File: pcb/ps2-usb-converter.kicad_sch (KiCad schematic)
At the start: 14 parts, among them J1 Mini-DIN-6

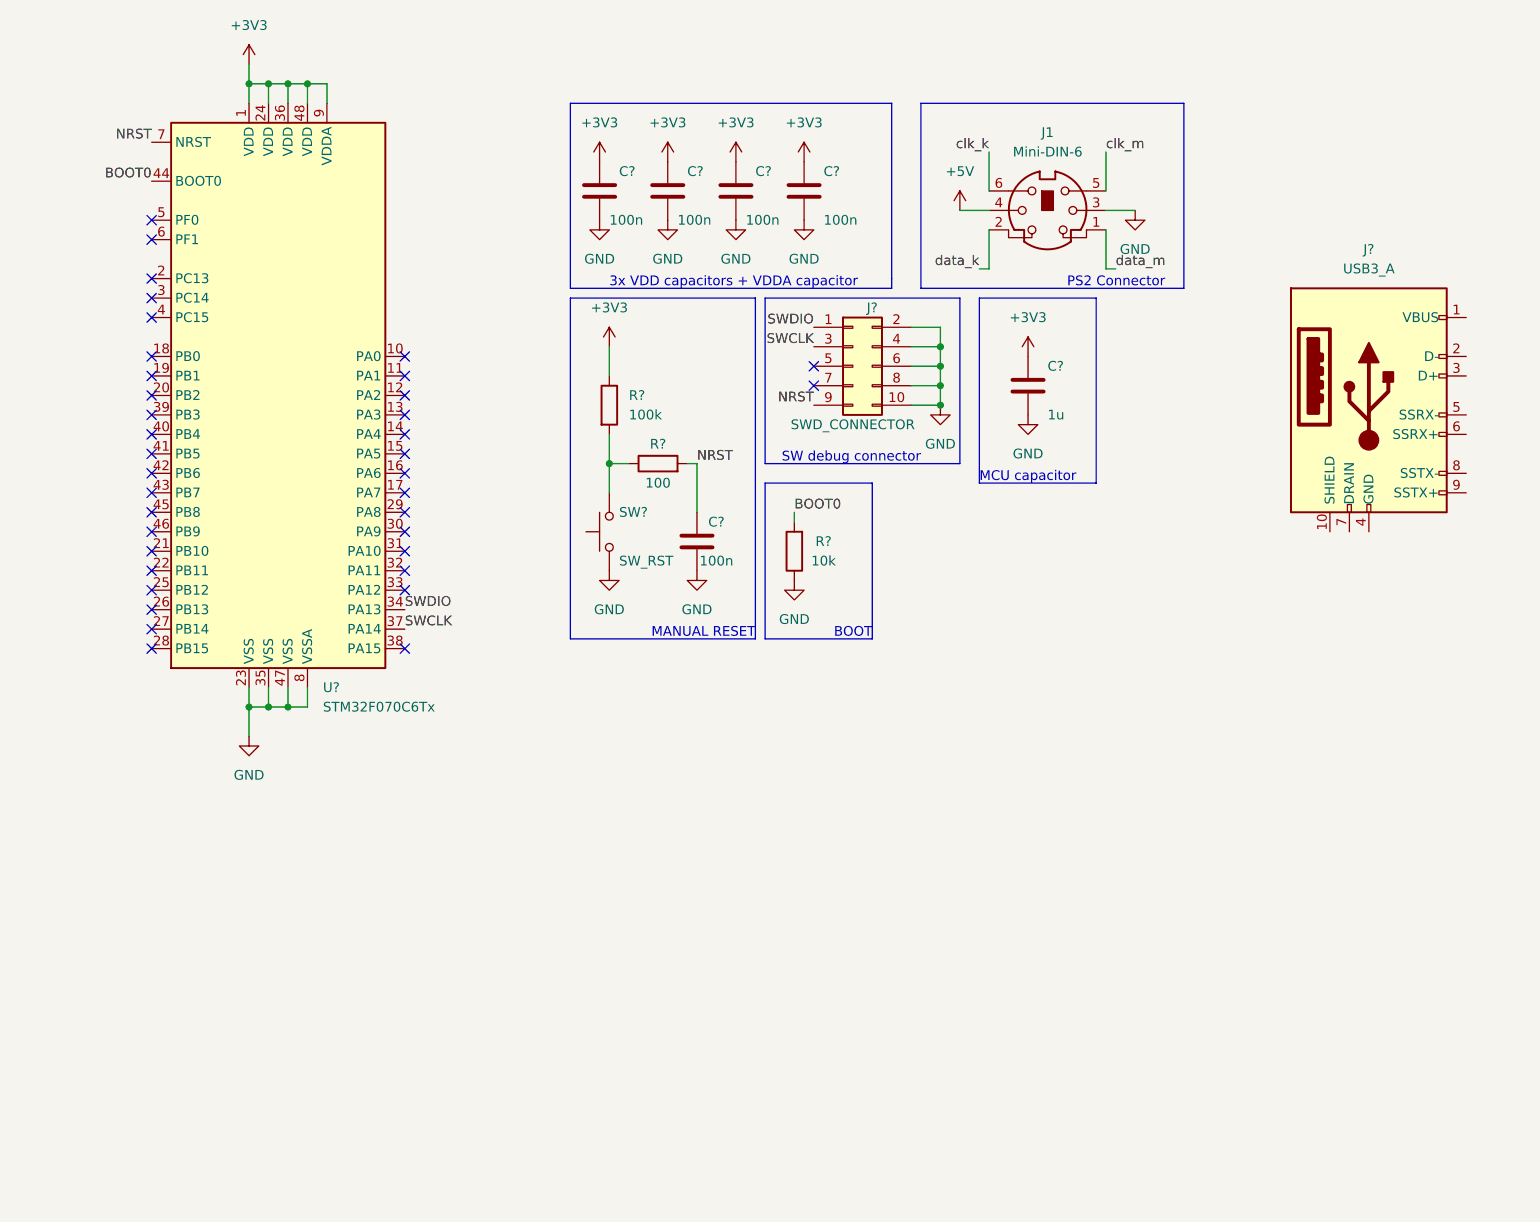
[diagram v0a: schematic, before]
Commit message: Add oscillator, power supply and usb connector to board
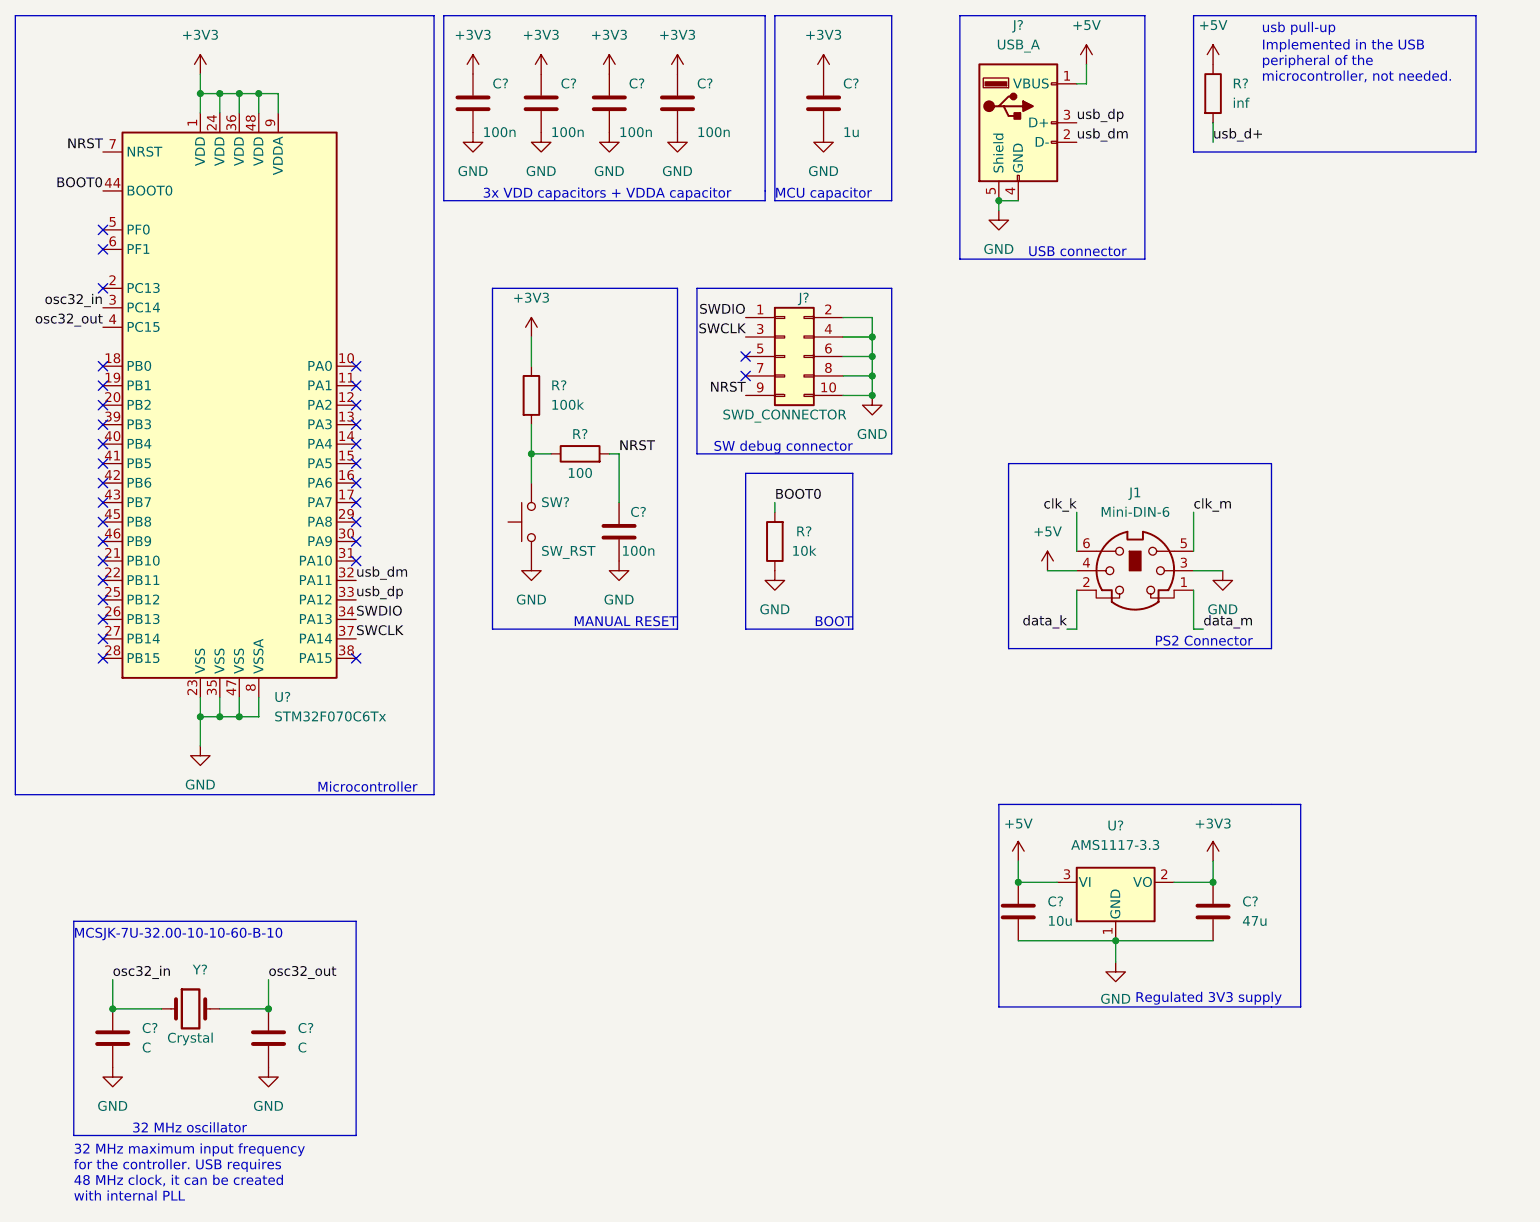
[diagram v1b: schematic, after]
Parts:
- removed J?: USB3_A, symbol Connector:USB3_A
- added C? (x2): C, symbol Device:C
- added C?: 10u, Capacitor_SMD:C_0805_2012Metric_Pad1.18x1.45mm_HandSolder, symbol Device:C
- added C?: 47u, Capacitor_SMD:C_0805_2012Metric_Pad1.18x1.45mm_HandSolder, symbol Device:C
- added J?: USB_A, symbol Connector:USB_A
- added R?: inf, symbol Device:R
- added U?: AMS1117-3.3, Package_TO_SOT_SMD:SOT-223-3_TabPin2, symbol Regulator_Linear:AMS1117-3.3
- added Y?: Crystal, symbol Device:Crystal
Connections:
- net +3V3: now also C?.1, U?.2 (VO)
- net +5V: now also C?.1, J?.1 (VBUS), R?.1, U?.3 (VI)
- net GND: now also C?.2, C?.2, C?.2, C?.2, J?.4 (GND), J?.5 (Shield), U?.1 (GND)
- net osc32_in: now reaches U?.3 (PC14)
- net osc32_in: now also C?.1, Y?.1
- net usb_dm: now reaches U?.32 (PA11)
- net usb_dm: now also J?.2 (D-)
- net usb_dp: now reaches U?.33 (PA12)
- net usb_dp: now also J?.3 (D+)
- net osc32_out: now reaches U?.4 (PC15)
- net osc32_out: now also C?.1, Y?.2
- new net usb_d+: R?.2
- no-connect marks 37 -> 33
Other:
- note added: "32 MHz maximum input frequency for the controller. USB requires 48 MHz clock, it can be created with internal PLL"
- note added: "32 MHz oscillator"
- note added: "Implemented in the USB peripheral of the microcontroller, not needed."
- note added: "MCSJK-7U-32.00-10-10-60-B-10"
- note added: "Microcontroller"
- note added: "Regulated 3V3 supply"
- note added: "USB connector"
- note added: "usb pull-up"
- moved on the sheet: C?, J1, J?, R?, SW?, U?

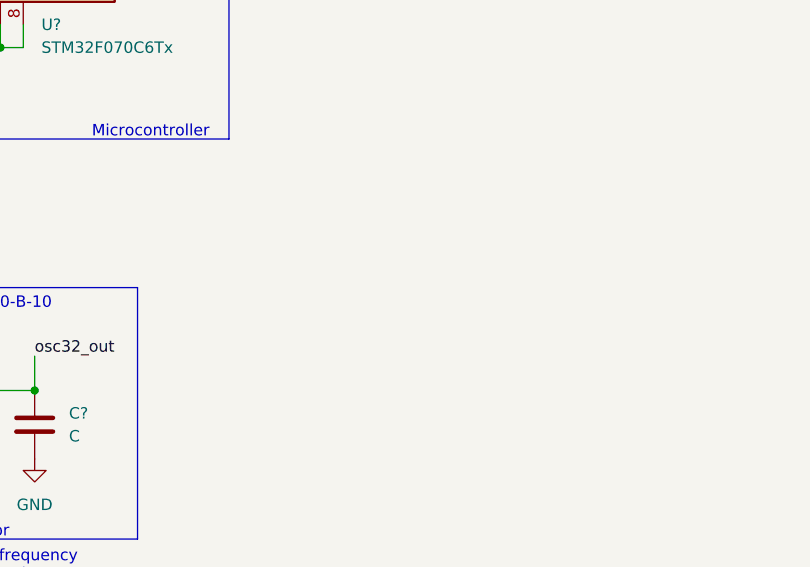
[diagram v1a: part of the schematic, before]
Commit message: Add user led to schematic
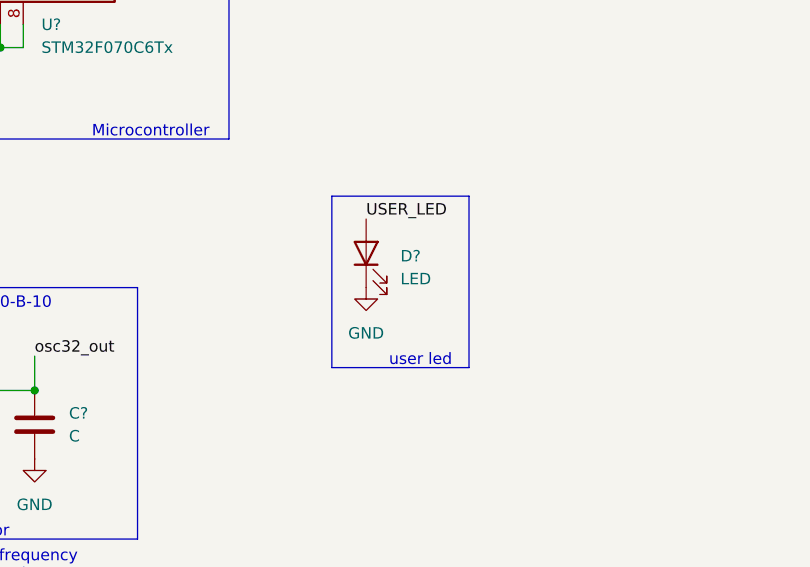
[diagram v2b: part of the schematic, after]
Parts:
- added D?: LED, symbol Device:LED
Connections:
- net GND: now also D?.1 (K)
- new net USER_LED: D?.2 (A)
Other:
- note added: "user led"
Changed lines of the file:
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@@
+    (stroke (width 0) (type default) (color 0 0 0 0))
+  )
+  (polyline (pts (xy 83.82 124.46) (xy 99.06 124.46))
     (stroke (width 0) (type default) (color 0 0 0 0))
   )
@@
     (stroke (width 0) (type default) (color 0 0 0 0))
   )
+  (polyline (pts (xy 83.82 143.51) (xy 83.82 124.46))
+    (stroke (width 0) (type default) (color 0 0 0 0))
+  )
   (wire (pts (xy 168.91 129.54) (xy 173.99 129.54))
     (stroke (width 0) (type default) (color 0 0 0 0))
@@
     (stroke (width 0) (type default) (color 0 0 0 0))
   )
+  (polyline (pts (xy 99.06 124.46) (xy 99.06 143.51))
+    (stroke (width 0) (type default) (color 0 0 0 0))
+  )
   (polyline (pts (xy 165.1 16.51) (xy 165.1 48.26))
     (stroke (width 0) (type default) (color 0 0 0 0))
   )
   (polyline (pts (xy 140.97 48.26) (xy 140.97 16.51))
+    (stroke (width 0) (type default) (color 0 0 0 0))
+  )
+  (polyline (pts (xy 83.82 143.51) (xy 99.06 143.51))
     (stroke (width 0) (type default) (color 0 0 0 0))
   )
@@
     (effects (font (size 1.27 1.27)) (justify left bottom))
   )
+  (text "user led" (at 90.17 143.51 0)
+    (effects (font (size 1.27 1.27)) (justify left bottom))
+  )
   (text "Microcontroller" (at 57.15 118.11 0)
+    (effects (font (size 1.27 1.27)) (justify left bottom))
+  )
+  (label "USER_LED" (at 87.63 127 0)
     (effects (font (size 1.27 1.27)) (justify left bottom))
   )
@@
     (pin "1")
   )
+  (symbol (lib_id "power:GND") (at 87.63 134.62 0) (unit 1)
+    (in_bom yes) (on_board yes) (fields_autoplaced)
+    (property "Reference" "#PWR?" (id 0) (at 87.63 140.97 0)
+      (effects (font (size 1.27 1.27)) hide)
+    )
+    (property "Value" "GND" (id 1) (at 87.63 139.7 0))
+    (property "Footprint" "" (id 2) (at 87.63 134.62 0)
+      (effects (font (size 1.27 1.27)) hide)
+    )
+    (property "Datasheet" "" (id 3) (at 87.63 134.62 0)
+      (effects (font (size 1.27 1.27)) hide)
+    )
+    (pin "1")
+  )
   (symbol (lib_id "power:GND") (at 96.52 87.63 0) (unit 1)
     (in_bom yes) (on_board yes) (fields_autoplaced)
@@
     )
     (pin "1")
+  )
+  (symbol (lib_id "Device:LED") (at 87.63 130.81 90) (unit 1)
+    (in_bom yes) (on_board yes) (fields_autoplaced)
+    (property "Reference" "D?" (id 0) (at 91.44 131.1274 90)
+      (effects (font (size 1.27 1.27)) (justify right))
+    )
+    (property "Value" "LED" (id 1) (at 91.44 133.6674 90)
+      (effects (font (size 1.27 1.27)) (justify right))
+    )
+    (property "Footprint" "" (id 2) (at 87.63 130.81 0)
+      (effects (font (size 1.27 1.27)) hide)
+    )
+    (property "Datasheet" "~" (id 3) (at 87.63 130.81 0)
+      (effects (font (size 1.27 1.27)) hide)
+    )
+    (pin "1")
+    (pin "2")
   )
   (symbol (lib_id "power:+5V") (at 173.99 22.86 0) (unit 1)
@@
       (reference "#PWR?") (unit 1) (value "GND") (footprint "")
     )
+    (path "/76f24aeb-19e4-46b8-b159-7e8a6720e158"
+      (reference "#PWR?") (unit 1) (value "GND") (footprint "")
+    )
     (path "/7dc509a6-01e7-46b7-86de-9de398dc9eda"
       (reference "#PWR?") (unit 1) (value "GND") (footprint "")
@@
       (reference "C?") (unit 1) (value "100n") (footprint "Capacitor_SMD:C_0805_2012Metric_Pad1.18x1.45mm_HandSolder")
     )
+    (path "/aabbb582-6a87-45eb-8ae9-d6a17d063591"
+      (reference "D?") (unit 1) (value "LED") (footprint "")
+    )
     (path "/cb05089f-05fe-4735-bfd7-bc3458e73618"
